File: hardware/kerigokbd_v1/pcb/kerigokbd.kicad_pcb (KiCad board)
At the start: 2 copper layers, 139.5 x 92 mm, 82 parts, among them J1 USB4520-03-0-A, J2 SDA SCL 5V GND, J3 SWC SWD GND, J4 SJ-3501-SMT-TR, SW1 SW_Push, SW10 SW_Push, SW11 SW_Push, SW12 SW_Push, SW13 SW_Push, SW14 SW_Push, SW15 SW_Push, SW16 SW_Push, SW17 SW_Push, SW18 SW_Push, SW19 SW_Push, SW2 SW_Push, SW20 SW_Push, SW21 SW_Push, SW22 SW_Push, SW23 SW_Push, SW24 SW_Push, SW3 SW_Push, SW4 SW_Push, SW5 SW_Push, SW6 SW_Push, SW7 SW_Push, SW8 SW_Push, SW9 SW_Push, U1 TLV75533PDBVR, U2 RP2040, U3 W25Q16JVUXIQ, Y1 12MHz

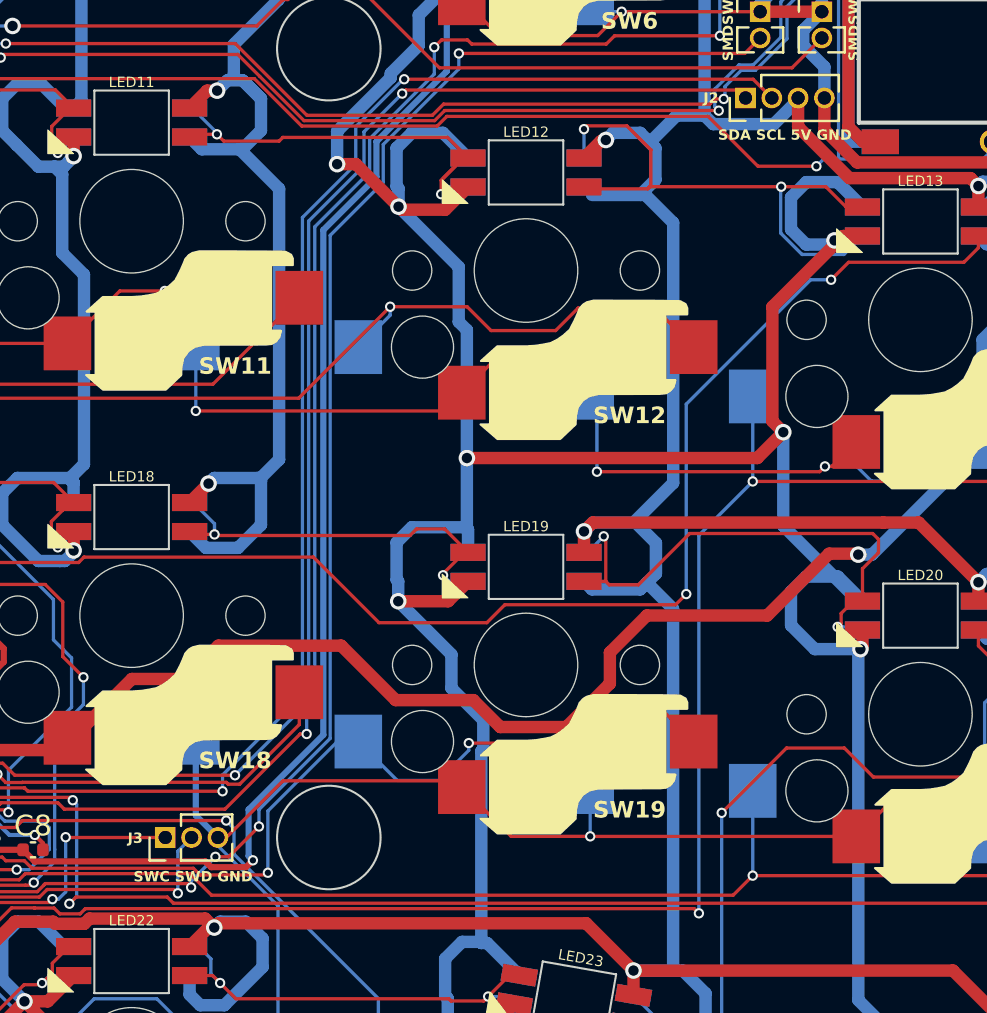
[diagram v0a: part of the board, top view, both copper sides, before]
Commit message: update kicad 3d path
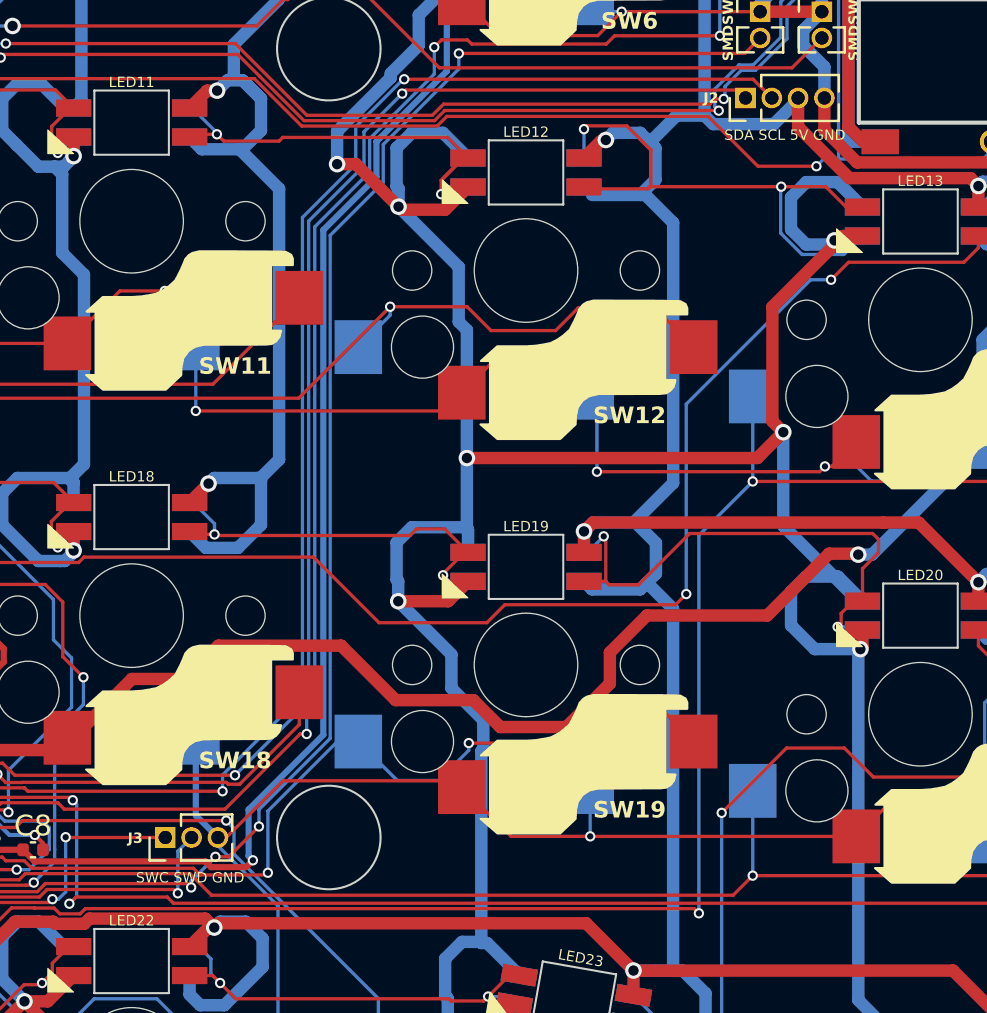
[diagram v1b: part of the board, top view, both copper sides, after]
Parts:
- J2: value SDA SCL 5V GND -> Conn_01x04
- J3: value SWC SWD GND -> Conn_01x03
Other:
- board text added: "SDA SCL 5V GND"
- board text added: "SWC SWD GND"

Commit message: update pcb
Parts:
- added ZD2: NSR0520V2T5G, Diode_SMD:D_SOD-523, F.Cu at (135.0, 32.4)
- J2: value Conn_01x04 -> I2C
- J3: value Conn_01x03 -> SWD
- SW1, SW10, SW11, SW12, SW13, SW14, SW15, SW16, SW17, SW18, SW19, SW2, SW20, SW21, SW22, SW23, SW24, SW3, SW4, SW5, SW6, SW7, SW8, SW9: value SW_Push -> Key_SW
- moved R3 7.04 mm to (147.5, 31.7), turned to 180 degrees
- moved R1 4.35 mm to (147.5, 32.7), turned to 180 degrees
- moved SMDSW1 3.65 mm to (134.4, 39.6)
- moved J4 1.19 mm to (148.8, 39.0)
- moved SMDSW2 1.08 mm to (134.4, 37.1)
- moved J2 0.24 mm to (131.9, 40.9), turned to 180 degrees
- renumbered JP2 to JP1, JP1 to JP2
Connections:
- J2 pad 3: +5V -> +3V3
- J3 pad 2: /SWD -> GND
- J3 pad 3: GND -> /SWD
- J4 pad R: /TX -> /SERIAL
- U2 pad 2: /TX -> /LED
- U2 pad 37: /LED -> /SPLIT_HAND
- U2 pad 38: /USB_VBUS_PIN -> /SDA
- U2 pad 39: /SPLIT_HAND -> /SCL
- U2 pad 40: /SCL -> /USB_VBUS_PIN
- U2 pad 41: /SDA -> /SERIAL
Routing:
- net /TX: track 110.0 -> 0.00 mm, vias 3 -> 0
- net /SERIAL: track 0.00 -> 109.9 mm, vias 0 -> 5
- net +5V: track 736.2 -> 722.5 mm
- net /LED: track 125.8 -> 113.6 mm
- net +3V3: track 135.1 -> 144.3 mm, vias 4 -> 5
- net Net-(J1-CC2): track 22.4 -> 13.6 mm
- net GND: track 854.7 -> 863.2 mm
- net Net-(J1-CC1): track 17.2 -> 12.4 mm
- net /SWD: track 17.0 -> 19.5 mm
- net /D+: track 101.4 -> 103.7 mm, vias 6 -> 8
- net /KEY18: track 33.0 -> 30.9 mm
- net Net-(U2-RUN): track 75.0 -> 77.0 mm, vias 4 -> 2
- net /SCL: track 69.0 -> 67.8 mm
- net /D-: track 98.7 -> 99.8 mm, vias 5 -> 7
- net /SPLIT_HAND: track 62.9 -> 61.8 mm
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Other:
- outline, holes or cut-outs redrawn
- board text added: "2025.02.08"
- board text added: "KERI's Lab KERIgoKBD v1.1"
- board text added: "Right"
- board text added: "SDA SCL 3V GND"
- board text added: "SWC GND SWD"
- board text removed: "2024.12.29"
- board text removed: "KERI's Lab KERIgoKBD v1"
- board text removed: "SDA SCL 5V GND"
- board text removed: "SWC SWD GND"

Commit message: update PCB v2026.02.22a
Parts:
- removed JP1: LED_EN, Jumper:SolderJumper-2_P1.3mm_Bridged_RoundedPad1.0x1.5mm
- removed ZD2: NSR0520V2T5G, Diode_SMD:D_SOD-523
- J1: moved to F.Cu
- J4: footprint kbd_local:PJ-398A-5A_PJ-399B-6A-dual -> kbd_local:SJ-3501-SMT-TR-dual; moved to F.Cu
- moved JP2 19.7 mm to (128.0, 79.1)
- moved C14 4.91 mm to (81.2, 78.5)
- moved C16 4.91 mm to (75.8, 78.5)
- moved R7 4.91 mm to (78.5, 80.9)
- moved Y1 4.91 mm to (78.5, 78.5)
- moved J3 4.74 mm to (108.4, 76.6)
- moved R5 4.20 mm to (93.4, 66.7)
- moved R6 4.20 mm to (94.3, 66.7)
- moved C5 3.54 mm to (91.4, 69.8)
- moved C4 3.45 mm to (90.6, 69.8)
- moved R4 2.38 mm to (133.5, 35.0)
- moved ZD1 2.29 mm to (133.5, 32.7)
- moved R2 2.22 mm to (133.5, 33.8)
- moved C1 2.10 mm to (131.0, 30.5)
- moved C2 2.10 mm to (131.1, 28.6)
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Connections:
- J1 pad B6: /D+ -> unconnected-(J1-D+-PadB6)
- J1 pad B7: /D- -> unconnected-(J1-D--PadB7)
- J4 pad R: /SERIAL -> GND
- J4 pad S: GND -> +5V
- J4 pad T: +5V -> /SERIAL
- LED1 pad 3: /LED_GND -> GND
- LED10 pad 3: /LED_GND -> GND
- LED11 pad 3: /LED_GND -> GND
- LED12 pad 3: /LED_GND -> GND
- LED13 pad 3: /LED_GND -> GND
- LED14 pad 3: /LED_GND -> GND
- LED15 pad 3: /LED_GND -> GND
- LED16 pad 3: /LED_GND -> GND
- LED17 pad 3: /LED_GND -> GND
- LED18 pad 3: /LED_GND -> GND
- LED19 pad 3: /LED_GND -> GND
- LED2 pad 3: /LED_GND -> GND
- LED20 pad 3: /LED_GND -> GND
- LED21 pad 3: /LED_GND -> GND
- LED22 pad 3: /LED_GND -> GND
- LED23 pad 3: /LED_GND -> GND
- LED24 pad 3: /LED_GND -> GND
- LED3 pad 3: /LED_GND -> GND
- LED4 pad 3: /LED_GND -> GND
- LED5 pad 3: /LED_GND -> GND
- LED6 pad 3: /LED_GND -> GND
- LED7 pad 3: /LED_GND -> GND
- LED8 pad 3: /LED_GND -> GND
- LED9 pad 3: /LED_GND -> GND
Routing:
- net /LED_GND: track 730.4 -> 0.00 mm, vias 31 -> 0
- net GND: track 863.2 -> 1400.1 mm, vias 36 -> 33
- net +3V3: track 144.3 -> 182.6 mm
- net /KEY15: track 60.8 -> 97.1 mm, vias 3 -> 6
- net +5V: track 722.5 -> 750.4 mm, vias 27 -> 24
- net /LED: track 113.6 -> 141.0 mm, vias 4 -> 2
- net /SPLIT_HAND: track 61.8 -> 37.2 mm, vias 2 -> 0
- net /KEY14: track 91.5 -> 113.5 mm, vias 3 -> 4
- net /KEY11: track 50.8 -> 72.7 mm
- net Net-(LED16-DOUT): track 35.2 -> 18.4 mm
- net /SERIAL: track 109.9 -> 93.6 mm, vias 5 -> 6
- net Net-(LED13-DOUT): track 159.8 -> 144.4 mm, vias 4 -> 2
- net /D+: track 103.7 -> 89.0 mm, vias 8 -> 4
- net /KEY17: track 50.1 -> 37.5 mm
- net Net-(U2-RUN): track 77.0 -> 88.4 mm
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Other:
- board size 139.5 x 92 mm -> 134.8 x 87.7 mm
- board text added: "KERI's Lab KERIgoKBD v1.2 PCB v2026.02.22a"
- board text added: "RST"
- board text removed: "2025.02.08"
- board text removed: "KERI's Lab KERIgoKBD v1.1"
- board text removed: "RESET"
